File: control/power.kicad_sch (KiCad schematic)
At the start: 14 parts, among them J2 Screw_Terminal_01x03, SW1 SW_DPDT_x2, T1 DST-5-36, U1 AP63205WU, U2 TLV1117-33

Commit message: Component Selection
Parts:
- C1: value 10m -> 1m; footprint (none) -> Capacitor_SMD:CP_Elec_16x17.5; PN (none) -> MAL214699008E3
- C2: footprint (none) -> Capacitor_SMD:C_0402_1005Metric_Pad0.74x0.62mm_HandSolder; PN (none) -> CGA2B3X7R1V104K050BB
- C3: footprint (none) -> Capacitor_SMD:C_0402_1005Metric_Pad0.74x0.62mm_HandSolder; PN (none) -> GCM155R71C104KA55D
- C4: footprint (none) -> Capacitor_Tantalum_SMD:CP_EIA-3528-21_Kemet-B_Pad1.50x2.35mm_HandSolder; PN (none) -> T495B226K016ATE600
- C5: footprint (none) -> Capacitor_SMD:C_1206_3216Metric_Pad1.33x1.80mm_HandSolder; PN (none) -> GRM31CZ71C226ME15L
- C6: footprint (none) -> Capacitor_SMD:C_0603_1608Metric_Pad1.08x0.95mm_HandSolder; PN (none) -> CGA3E1X7R1C105K080AC
- C7: footprint (none) -> Capacitor_SMD:C_0402_1005Metric_Pad0.74x0.62mm_HandSolder; PN (none) -> GRT155R70J105KE01D
- D2: PN (none) -> ABS10A-13
- J2: footprint (none) -> TerminalBlock_TE-Connectivity:TerminalBlock_TE_282834-3_1x03_P2.54mm_Horizontal; PN (none) -> 282834-3
- L1: footprint (none) -> Inductor_SMD:L_Coilcraft_MSS1278-XXX; PN (none) -> MSS1278-473MLD
- T1: PN (none) -> DST-5-36
- U1: PN (none) -> AP63205WU-7
- U2: footprint (none) -> Package_TO_SOT_SMD:SOT-223-3_TabPin2; PN (none) -> TLV1117-33CDCYR
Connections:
- net LINE: now also SW1.4 (A); no longer SW1.6 (C)
- net NEUT: now also SW1.1 (A); no longer SW1.3 (C)
- new net: SW1.3 (C), SW1.6 (C)
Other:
- moved on the sheet: J2, SW1A, SW1B

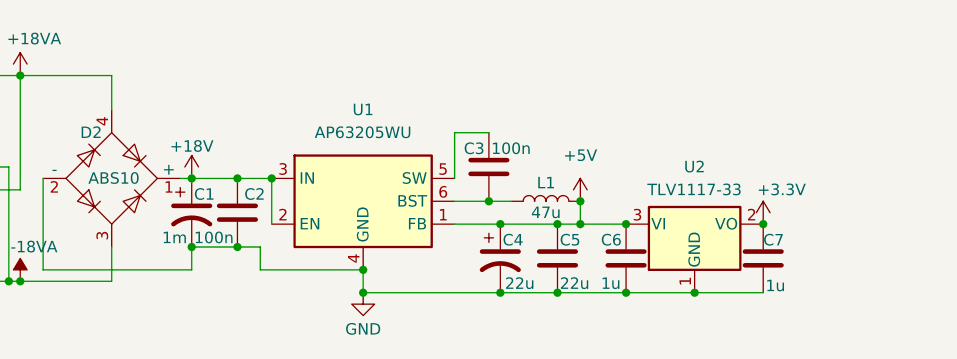
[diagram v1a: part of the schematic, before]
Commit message: Reduce ripple voltage
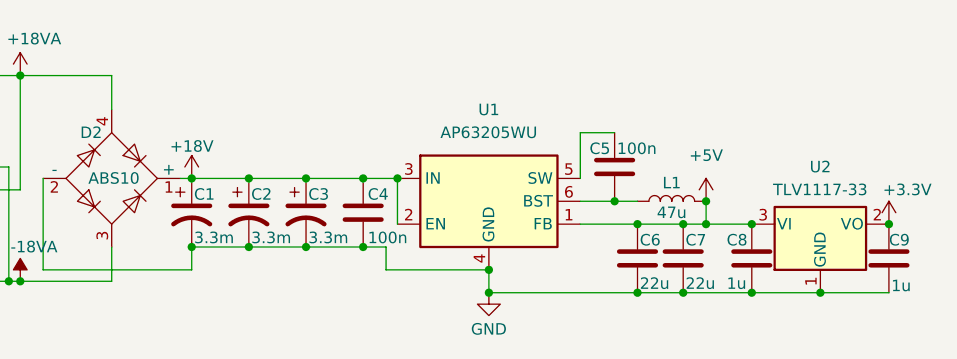
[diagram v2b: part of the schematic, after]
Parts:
- removed C4: 22u, Capacitor_Tantalum_SMD:CP_EIA-3528-21_Kemet-B_Pad1.50x2.35mm_HandSolder, symbol Device:C_Polarized_US
- added C2, C3: 3.3m, Capacitor_THT:CP_Radial_D18.0mm_P7.50mm, symbol Device:C_Polarized_US
- added C6: 22u, Capacitor_SMD:C_1206_3216Metric_Pad1.33x1.80mm_HandSolder, symbol Device:C
- C1: value 1m -> 3.3m; footprint Capacitor_SMD:CP_Elec_16x17.5 -> Capacitor_THT:CP_Radial_D18.0mm_P7.50mm; PN MAL214699008E3 -> MAL215051332E3
- renumbered C2 to C4, C3 to C5, C5 to C7, C6 to C8, C7 to C9
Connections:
- net +18V: now also C2.1, C3.1
- net +5V: now also C6.1
- net GND: now also C2.2, C3.2, C6.2
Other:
- moved on the sheet: C4, C5, C7, C8, C9, L1, U1, U2

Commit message: Cleanup/organization
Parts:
- removed C8: 1u, Capacitor_SMD:C_0603_1608Metric_Pad1.08x0.95mm_HandSolder, symbol Device:C
- removed C9: 1u, Capacitor_SMD:C_0402_1005Metric_Pad0.74x0.62mm_HandSolder, symbol Device:C
- removed J2: Screw_Terminal_01x03, TerminalBlock_TE-Connectivity:TerminalBlock_TE_282834-3_1x03_P2.54mm_Horizontal, symbol Connector:Screw_Terminal_01x03
- removed U2: TLV1117-33, Package_TO_SOT_SMD:SOT-223-3_TabPin2, symbol Regulator_Linear:TLV1117-33
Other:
- moved on the sheet: C1, C2, C3, C4, C5, C6, C7, D2, L1, SW1A, SW1B, T1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

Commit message: ???
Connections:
- net at C5.1, U1.5 (SW): now also L1.1
- net at C5.2, U1.6 (BST): no longer L1.1
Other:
- moved on the sheet: C6, C7, L1
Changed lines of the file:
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@@
 	)
 	(junction
-		(at 198.12 99.06)
-		(diameter 0)
-		(color 0 0 0 0)
-	)
-	(junction
-		(at 187.96 99.06)
+		(at 195.58 99.06)
 		(diameter 0)
 		(color 0 0 0 0)
@@
 	)
 	(junction
+		(at 189.23 109.22)
+		(diameter 0)
+		(color 0 0 0 0)
+	)
+	(junction
+		(at 195.58 91.44)
+		(diameter 0)
+		(color 0 0 0 0)
+	)
+	(junction
+		(at 184.15 101.6)
+		(diameter 0)
+		(color 0 0 0 0)
+	)
+	(junction
 		(at 160.02 96.52)
 		(diameter 0)
@@
 	)
 	(junction
-		(at 190.5 101.6)
+		(at 184.15 109.22)
+		(diameter 0)
+		(color 0 0 0 0)
+	)
+	(junction
+		(at 189.23 101.6)
 		(diameter 0)
 		(color 0 0 0 0)
@@
 	)
 	(junction
+		(at 187.96 91.44)
+		(diameter 0)
+		(color 0 0 0 0)
+	)
+	(junction
 		(at 121.92 107.95)
 		(diameter 0)
@@
 		(color 0 0 0 0)
 	)
-	(junction
-		(at 195.58 109.22)
-		(diameter 0)
-		(color 0 0 0 0)
-	)
-	(junction
-		(at 195.58 101.6)
-		(diameter 0)
-		(color 0 0 0 0)
-	)
-	(junction
-		(at 190.5 109.22)
-		(diameter 0)
-		(color 0 0 0 0)
-	)
 	(wire
 		(pts
@@
 	(wire
 		(pts
-			(xy 184.15 101.6) (xy 190.5 101.6)
-		)
-		(stroke
-			(width 0)
-			(type default)
-		)
-	)
-	(wire
-		(pts
-			(xy 198.12 99.06) (xy 200.66 99.06)
+			(xy 195.58 99.06) (xy 198.12 99.06)
 		)
 		(stroke
@@
 	(wire
 		(pts
-			(xy 190.5 109.22) (xy 195.58 109.22)
-		)
-		(stroke
-			(width 0)
-			(type default)
-		)
-	)
-	(wire
-		(pts
-			(xy 190.5 99.06) (xy 187.96 99.06)
-		)
-		(stroke
-			(width 0)
-			(type default)
-		)
-	)
-	(wire
-		(pts
 			(xy 140.97 104.14) (xy 147.32 104.14)
 		)
@@
 	(wire
 		(pts
-			(xy 195.58 101.6) (xy 198.12 101.6)
-		)
-		(stroke
-			(width 0)
-			(type default)
-		)
-	)
-	(wire
-		(pts
 			(xy 184.15 99.06) (xy 187.96 99.06)
 		)
@@
 	(wire
 		(pts
-			(xy 198.12 99.06) (xy 198.12 101.6)
+			(xy 195.58 99.06) (xy 195.58 101.6)
 		)
 		(stroke
@@
 	(wire
 		(pts
-			(xy 190.5 101.6) (xy 195.58 101.6)
-		)
-		(stroke
-			(width 0)
-			(type default)
-		)
-	)
-	(wire
-		(pts
-			(xy 173.99 109.22) (xy 190.5 109.22)
+			(xy 184.15 109.22) (xy 189.23 109.22)
+		)
+		(stroke
+			(width 0)
+			(type default)
+		)
+	)
+	(wire
+		(pts
+			(xy 173.99 109.22) (xy 184.15 109.22)
 		)
 		(stroke
@@
 	(wire
 		(pts
+			(xy 189.23 101.6) (xy 195.58 101.6)
+		)
+		(stroke
+			(width 0)
+			(type default)
+		)
+	)
+	(wire
+		(pts
 			(xy 120.65 107.95) (xy 121.92 107.95)
 		)
@@
 	(wire
 		(pts
+			(xy 184.15 101.6) (xy 189.23 101.6)
+		)
+		(stroke
+			(width 0)
+			(type default)
+		)
+	)
+	(wire
+		(pts
 			(xy 121.92 85.09) (xy 132.08 85.09)
 		)
@@
 	(wire
 		(pts
+			(xy 189.23 109.22) (xy 198.12 109.22)
+		)
+		(stroke
+			(width 0)
+			(type default)
+		)
+	)
+	(wire
+		(pts
 			(xy 87.63 93.98) (xy 87.63 99.06)
 		)
@@
 	(wire
 		(pts
-			(xy 195.58 109.22) (xy 200.66 109.22)
+			(xy 195.58 91.44) (xy 195.58 99.06)
 		)
 		(stroke
@@
 	(hierarchical_label "GND"
 		(shape output)
-		(at 200.66 109.22 0)
+		(at 198.12 109.22 0)
 		(fields_autoplaced yes)
 		(effects
@@
 	(hierarchical_label "+5V"
 		(shape output)
-		(at 200.66 99.06 0)
+		(at 198.12 99.06 0)
 		(fields_autoplaced yes)
 		(effects
@@
 		(dnp no)
 		(property "Reference" "C5"
-			(at 185.166 93.218 0)
+			(at 184.912 97.536 0)
 			(effects
 				(font
@@
 		)
 		(property "Value" "100n"
-			(at 188.214 93.218 0)
+			(at 188.976 97.536 0)
 			(effects
 				(font
@@
 	(symbol
 		(lib_id "power:+5V")
-		(at 198.12 99.06 0)
+		(at 195.58 91.44 0)
 		(unit 1)
 		(exclude_from_sim no)
@@
 		(fields_autoplaced yes)
 		(property "Reference" "#PWR015"
-			(at 198.12 102.87 0)
+			(at 195.58 95.25 0)
 			(effects
 				(font
@@
 		)
 		(property "Value" "+5V"
-			(at 198.12 93.98 0)
+			(at 195.58 86.36 0)
 			(effects
 				(font
@@
 		)
 		(property "Footprint" ""
-			(at 198.12 99.06 0)
+			(at 195.58 91.44 0)
 			(effects
 				(font
@@
 		)
 		(property "Datasheet" ""
-			(at 198.12 99.06 0)
+			(at 195.58 91.44 0)
 			(effects
 				(font
@@
 		)
 		(property "Description" "Power symbol creates a global label with name \"+5V\""
-			(at 198.12 99.06 0)
+			(at 195.58 91.44 0)
 			(effects
 				(font
@@
 	(symbol
 		(lib_id "Device:L")
-		(at 194.31 99.06 90)
+		(at 191.77 91.44 90)
 		(unit 1)
 		(exclude_from_sim no)
@@
 		(dnp no)
 		(property "Reference" "L1"
-			(at 194.31 97.028 90)
+			(at 191.77 89.408 90)
 			(effects
 				(font
@@
 		)
 		(property "Value" "47u"
-			(at 194.31 100.33 90)
+			(at 191.77 92.71 90)
 			(effects
 				(font
@@
 		)
 		(property "Footprint" "Inductor_SMD:L_Coilcraft_MSS1278-XXX"
-			(at 194.31 99.06 0)
+			(at 191.77 91.44 0)
 			(effects
 				(font
@@
 		)
 		(property "Datasheet" "~"
-			(at 194.31 99.06 0)
+			(at 191.77 91.44 0)
 			(effects
 				(font
@@
 		)
 		(property "Description" "Inductor"
-			(at 194.31 99.06 0)
+			(at 191.77 91.44 0)
 			(effects
 				(font
@@
 		)
 		(property "PN" "MSS1278-473MLD"
-			(at 194.31 99.06 0)
+			(at 191.77 91.44 0)
 			(effects
 				(font
@@
 	(symbol
 		(lib_id "Device:C")
-		(at 190.5 105.41 0)
+		(at 184.15 105.41 0)
 		(unit 1)
 		(exclude_from_sim no)
@@
 		(dnp no)
 		(property "Reference" "C6"
-			(at 190.754 103.378 0)
+			(at 184.404 103.378 0)
 			(effects
 				(font
@@
 		)
 		(property "Value" "22u"
-			(at 190.754 108.204 0)
+			(at 184.404 108.204 0)
 			(effects
 				(font
@@
 		)
 		(property "Footprint" "Capacitor_SMD:C_1206_3216Metric_Pad1.33x1.80mm_HandSolder"
-			(at 191.4652 109.22 0)
+			(at 185.1152 109.22 0)
 			(effects
 				(font
@@
 		)
 		(property "Datasheet" "~"
-			(at 190.5 105.41 0)
+			(at 184.15 105.41 0)
 			(effects
 				(font
@@
 		)
 		(property "Description" "Unpolarized capacitor"
-			(at 190.5 105.41 0)
+			(at 184.15 105.41 0)
 			(effects
 				(font
@@
 		)
 		(property "PN" "GRM31CZ71C226ME15L"
-			(at 190.5 105.41 0)
+			(at 184.15 105.41 0)
 			(effects
 				(font
@@
 	(symbol
 		(lib_id "Device:C")
-		(at 195.58 105.41 0)
+		(at 189.23 105.41 0)
 		(unit 1)
 		(exclude_from_sim no)
@@
 		(dnp no)
 		(property "Reference" "C7"
-			(at 195.834 103.378 0)
+			(at 189.484 103.378 0)
 			(effects
 				(font
@@
 		)
 		(property "Value" "22u"
-			(at 195.834 108.204 0)
+			(at 189.484 108.204 0)
 			(effects
 				(font
@@
 		)
 		(property "Footprint" "Capacitor_SMD:C_1206_3216Metric_Pad1.33x1.80mm_HandSolder"
-			(at 196.5452 109.22 0)
+			(at 190.1952 109.22 0)
 			(effects
 				(font
@@
 		)
 		(property "Datasheet" "~"
-			(at 195.58 105.41 0)
+			(at 189.23 105.41 0)
 			(effects
 				(font
@@
 		)
 		(property "Description" "Unpolarized capacitor"
-			(at 195.58 105.41 0)
+			(at 189.23 105.41 0)
 			(effects
 				(font
@@
 		)
 		(property "PN" "GRM31CZ71C226ME15L"
-			(at 195.58 105.41 0)
-			(effects
-				(font
+			(at 189.23 105.41 0)
+			(effects
+				(font

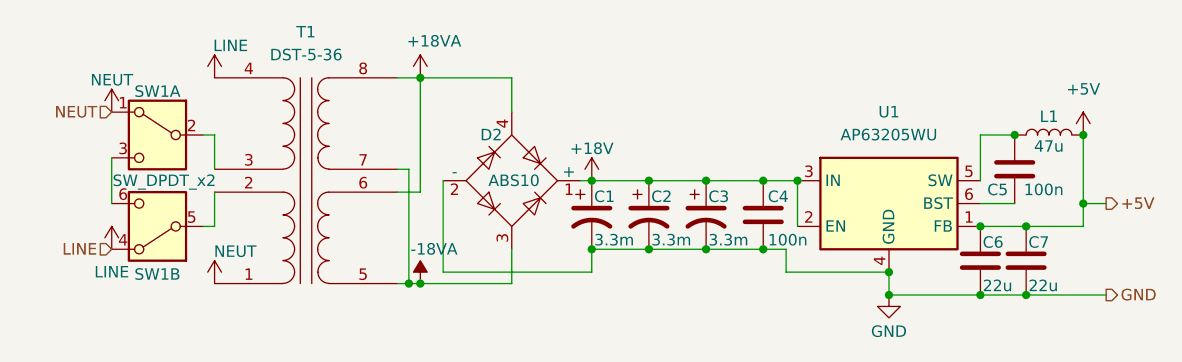
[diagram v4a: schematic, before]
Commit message: Daughterboard setup, labeling, and testpoints
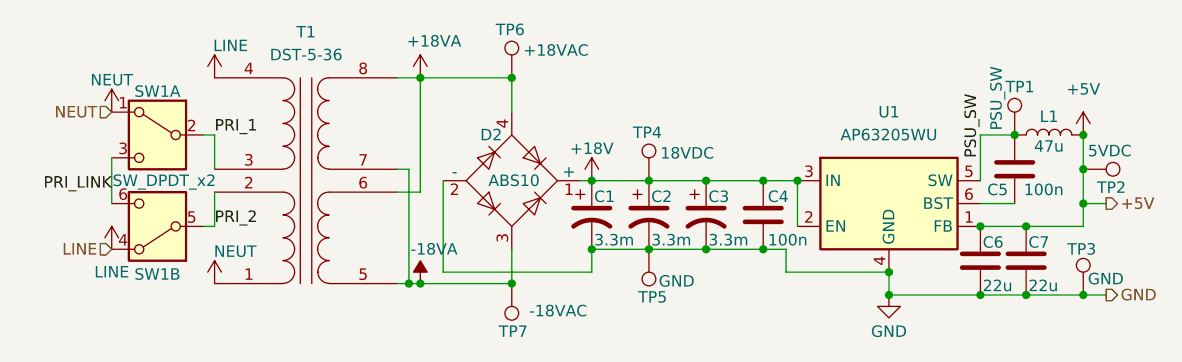
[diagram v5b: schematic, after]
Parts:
- added TP1: PSU_SW, symbol Connector:TestPoint
- added TP2: 5VDC, symbol Connector:TestPoint
- added TP3, TP5: GND, symbol Connector:TestPoint
- added TP4: 18VDC, symbol Connector:TestPoint
- added TP6: +18VAC, symbol Connector:TestPoint
- added TP7: -18VAC, symbol Connector:TestPoint
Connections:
- net +18V: now also TP4.1
- net +18VA: now also TP6.1
- net +5V: now also TP2.1
- net -18VA: now also TP7.1
- net GND: now also TP3.1, TP5.1
- net PSU_SW: now reaches C5.1, L1.1, U1.5 (SW)
- net PSU_SW: now also TP1.1
- net PRI_1: now reaches SW1.2 (B), T1.3
- net PRI_LINK: now reaches SW1.3 (C), SW1.6 (C)
- net PRI_2: now reaches SW1.5 (B), T1.2
